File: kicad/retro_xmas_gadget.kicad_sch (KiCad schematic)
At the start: 83 parts, among them J1 USB_C_Receptacle_USB2.0_16P, J2 SD_Card_Receptacle, J3 AudioJack3_SwitchTR, J4 Conn_01x18, J5 Conn_01x02, J6 Conn_01x03, J7 Conn_01x03, J8 Conn_01x07, Q1 UMH3N, Q2 SS8050, Q3 PMOS, SW1 RESET, SW10 SELECT, SW11 START, SW12 A, SW13 B, SW2 BOOT, SW3 KH-SS12F23-G6, SW4 UP, SW5 DOWN, SW6 LEFT, SW7 RIGHT, SW8 MENU, SW9 OPTION, U1 CP2102N-Axx-xQFN28, U2 ESP32-S3-WROOM-1, U4 XC6210B332MR, U5 TP4056

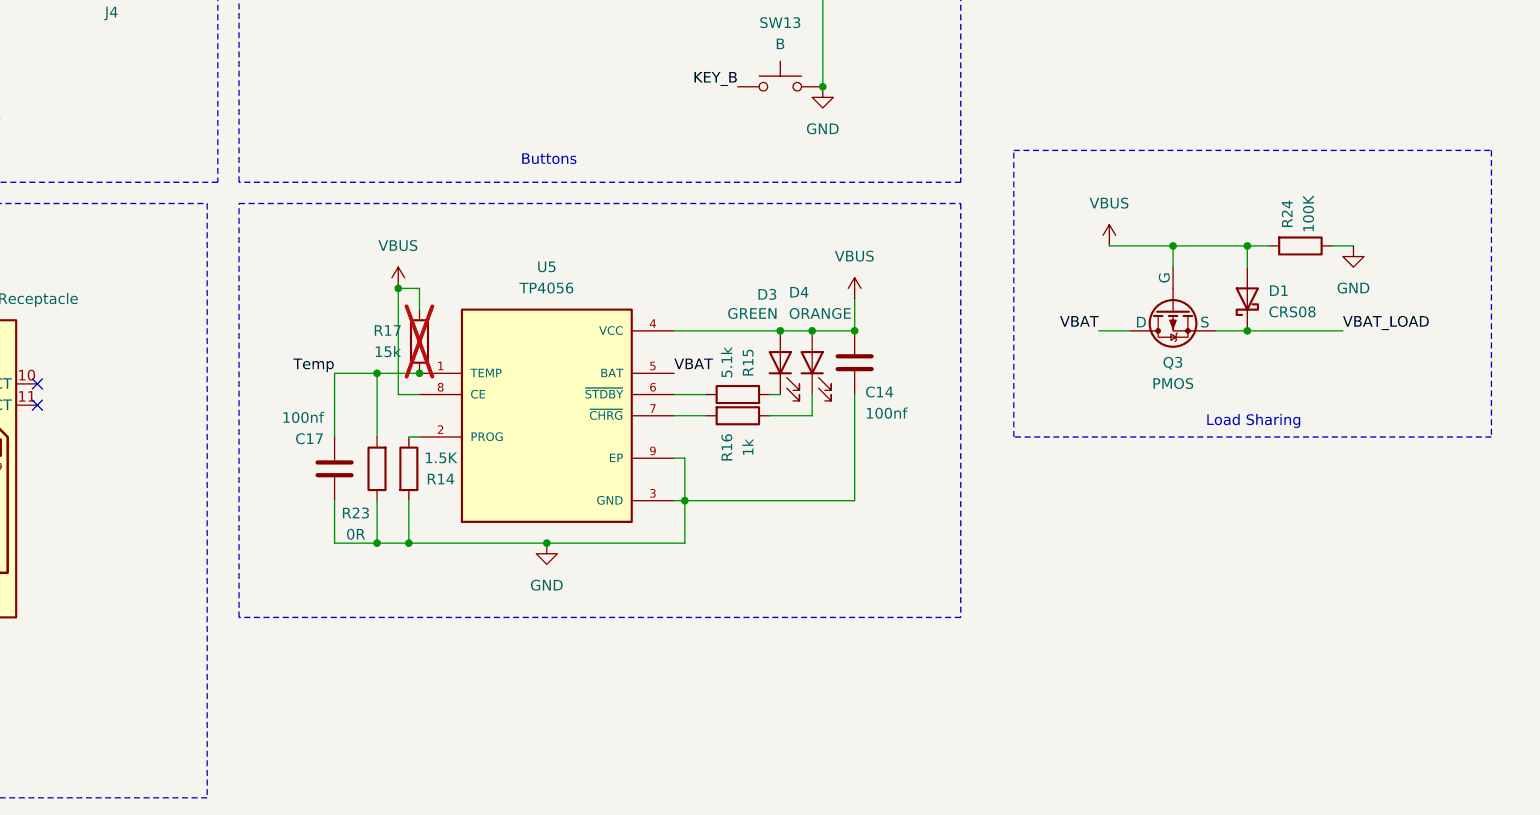
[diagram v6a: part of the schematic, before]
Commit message: footprint correction
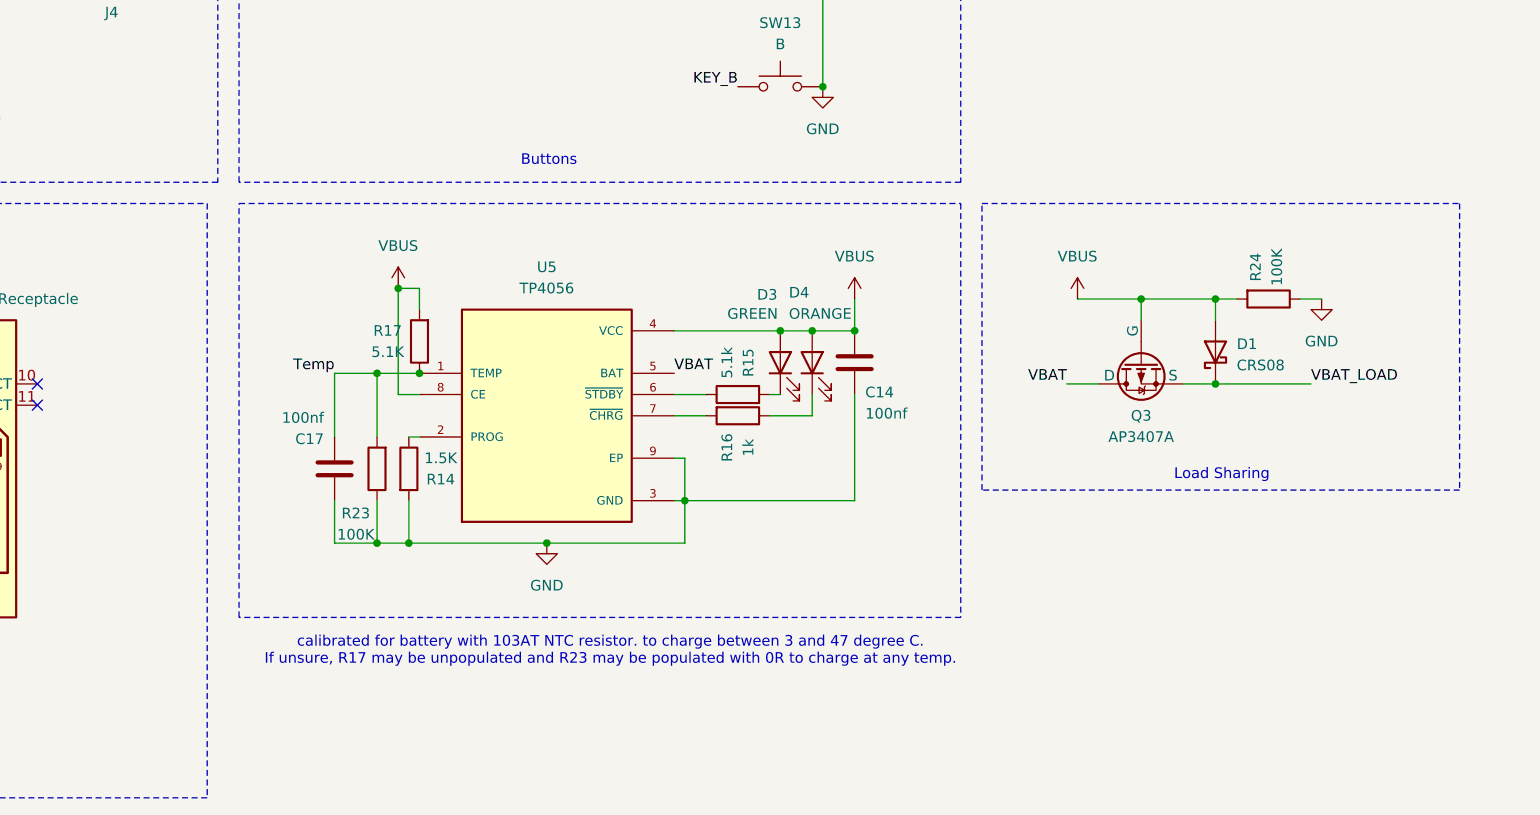
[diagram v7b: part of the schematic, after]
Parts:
- Q3: value PMOS -> AP3407A
- R17: value 15k -> 5.1K; now fitted
- R23: value 0R -> 100K
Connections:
- net VBAT: now also Q3.2 (D); no longer Q3.1 (D)
- net VBUS: now also Q3.1 (G); no longer Q3.2 (G)
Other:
- note added: "calibrated for battery with 103AT NTC resistor. to charge between 3 and 47 degree C. If unsure, R17 may be unpopulated and R23 may be populated with 0R to charge at any temp."
- moved on the sheet: D1, Q3, R24
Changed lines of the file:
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@@
 	)
 	(rectangle
-		(start 328.93 195.58)
-		(end 386.08 229.87)
+		(start 325.12 201.93)
+		(end 382.27 236.22)
 		(stroke
 			(width 0)
@@
 	(text "Load Sharing"
 		(exclude_from_sim no)
-		(at 357.632 228.092 0)
+		(at 353.822 234.442 0)
 		(effects
 			(font
@@
 		)
 	)
+	(text "calibrated for battery with 103AT NTC resistor. to charge between 3 and 47 degree C.\nIf unsure, R17 may be unpopulated and R23 may be populated with 0R to charge at any temp."
+		(exclude_from_sim no)
+		(at 280.67 255.524 0)
+		(effects
+			(font
+				(size 1.27 1.27)
+			)
+		)
+	)
 	(junction
 		(at 215.9 157.48)
@@
 	)
 	(junction
-		(at 356.87 217.17)
+		(at 353.06 223.52)
 		(diameter 0)
 		(color 0 0 0 0)
@@
 	)
 	(junction
-		(at 347.98 207.01)
+		(at 344.17 213.36)
 		(diameter 0)
 		(color 0 0 0 0)
@@
 	)
 	(junction
-		(at 356.87 207.01)
+		(at 353.06 213.36)
 		(diameter 0)
 		(color 0 0 0 0)
@@
 	(wire
 		(pts
-			(xy 369.57 207.01) (xy 367.03 207.01)
+			(xy 365.76 213.36) (xy 363.22 213.36)
 		)
 		(stroke
@@
 	(wire
 		(pts
-			(xy 356.87 207.01) (xy 347.98 207.01)
+			(xy 353.06 213.36) (xy 344.17 213.36)
 		)
 		(stroke
@@
 	(wire
 		(pts
-			(xy 347.98 207.01) (xy 347.98 209.55)
+			(xy 344.17 213.36) (xy 344.17 215.9)
 		)
 		(stroke
@@
 	(wire
 		(pts
-			(xy 340.36 207.01) (xy 347.98 207.01)
+			(xy 336.55 213.36) (xy 344.17 213.36)
 		)
 		(stroke
@@
 	(wire
 		(pts
-			(xy 359.41 207.01) (xy 356.87 207.01)
+			(xy 355.6 213.36) (xy 353.06 213.36)
 		)
 		(stroke
@@
 	(wire
 		(pts
-			(xy 356.87 209.55) (xy 356.87 207.01)
+			(xy 353.06 215.9) (xy 353.06 213.36)
 		)
 		(stroke
@@
 	(wire
 		(pts
-			(xy 353.06 217.17) (xy 356.87 217.17)
+			(xy 349.25 223.52) (xy 353.06 223.52)
 		)
 		(stroke
@@
 	(wire
 		(pts
-			(xy 356.87 217.17) (xy 368.3 217.17)
+			(xy 353.06 223.52) (xy 364.49 223.52)
 		)
 		(stroke
@@
 	(wire
 		(pts
-			(xy 342.9 217.17) (xy 339.09 217.17)
+			(xy 339.09 223.52) (xy 335.28 223.52)
 		)
 		(stroke
@@
 	)
 	(label "VBAT_LOAD"
-		(at 368.3 217.17 0)
+		(at 364.49 223.52 0)
 		(effects
 			(font
@@
 	)
 	(label "VBAT"
-		(at 339.09 217.17 180)
+		(at 335.28 223.52 180)
 		(effects
 			(font
@@
 	(symbol
 		(lib_id "power:VBUS")
-		(at 340.36 207.01 0)
+		(at 336.55 213.36 0)
 		(unit 1)
 		(exclude_from_sim no)
@@
 		(fields_autoplaced yes)
 		(property "Reference" "#PWR035"
-			(at 340.36 210.82 0)
+			(at 336.55 217.17 0)
 			(effects
 				(font
@@
 		)
 		(property "Value" "VBUS"
-			(at 340.36 201.93 0)
+			(at 336.55 208.28 0)
 			(effects
 				(font
@@
 		)
 		(property "Footprint" ""
-			(at 340.36 207.01 0)
+			(at 336.55 213.36 0)
 			(effects
 				(font
@@
 		)
 		(property "Datasheet" ""
-			(at 340.36 207.01 0)
+			(at 336.55 213.36 0)
 			(effects
 				(font
@@
 		)
 		(property "Description" "Power symbol creates a global label with name \"VBUS\""
-			(at 340.36 207.01 0)
+			(at 336.55 213.36 0)
 			(effects
 				(font
@@
 	(symbol
 		(lib_id "Device:R")
-		(at 363.22 207.01 270)
+		(at 359.41 213.36 270)
 		(unit 1)
 		(exclude_from_sim no)
@@
 		(dnp no)
 		(property "Reference" "R24"
-			(at 361.696 203.2 0)
+			(at 357.886 209.55 0)
 			(effects
 				(font
@@
 		)
 		(property "Value" "100K"
-			(at 364.236 203.2 0)
+			(at 360.426 209.55 0)
 			(effects
 				(font
@@
 		)
 		(property "Footprint" "Resistor_SMD:R_0603_1608Metric_Pad0.98x0.95mm_HandSolder"
-			(at 363.22 205.232 90)
+			(at 359.41 211.582 90)
 			(effects
 				(font
@@
 		)
 		(property "Datasheet" "~"
-			(at 363.22 207.01 0)
+			(at 359.41 213.36 0)
 			(effects
 				(font
@@
 		)
 		(property "Description" "Resistor"
-			(at 363.22 207.01 0)
+			(at 359.41 213.36 0)
 			(effects
 				(font
@@
 		(in_bom yes)
 		(on_board yes)
-		(dnp yes)
+		(dnp no)
 		(property "Reference" "R17"
 			(at 254 217.17 0)
@@
 			)
 		)
-		(property "Value" "15k"
+		(property "Value" "5.1K"
 			(at 254 219.71 0)
 			(effects
@@
 	(symbol
 		(lib_id "Device:D_Schottky")
-		(at 356.87 213.36 90)
+		(at 353.06 219.71 90)
 		(unit 1)
 		(exclude_from_sim no)
@@
 		(fields_autoplaced yes)
 		(property "Reference" "D1"
-			(at 359.41 212.4074 90)
+			(at 355.6 218.7574 90)
 			(effects
 				(font
@@
 		)
 		(property "Value" "CRS08"
-			(at 359.41 214.9474 90)
+			(at 355.6 221.2974 90)
 			(effects
 				(font
@@
 		)
 		(property "Footprint" "Diode_SMD:D_SOD-123"
-			(at 356.87 213.36 0)
+			(at 353.06 219.71 0)
 			(effects
 				(font
@@
 		)
 		(property "Datasheet" "~"
-			(at 356.87 213.36 0)
+			(at 353.06 219.71 0)
 			(effects
 				(font
@@
 		)
 		(property "Description" "Schottky diode"
-			(at 356.87 213.36 0)
+			(at 353.06 219.71 0)
 			(effects
 				(font
@@
 			)
 		)
-		(property "Value" "0R"
+		(property "Value" "100K"
 			(at 250.19 241.554 0)
 			(effects
@@
 	(symbol
 		(lib_id "Simulation_SPICE:PMOS")
-		(at 347.98 214.63 90)
+		(at 344.17 220.98 90)
 		(mirror x)
 		(unit 1)
@@
 		(dnp no)
 		(property "Reference" "Q3"
-			(at 347.98 220.98 90)
+			(at 344.17 227.33 90)
 			(effects
 				(font
@@
 			)
 		)
-		(property "Value" "PMOS"
-			(at 347.98 223.52 90)
+		(property "Value" "AP3407A"
+			(at 344.17 229.87 90)
 			(effects
 				(font
@@
 		)
 		(property "Footprint" "Package_TO_SOT_SMD:SOT-23_Handsoldering"
-			(at 345.44 219.71 0)
+			(at 341.63 226.06 0)
 			(effects
 				(font
@@
 		)
 		(property "Datasheet" "https://ngspice.sourceforge.io/docs/ngspice-html-manual/manual.xhtml#cha_MOSFETs"
-			(at 360.68 214.63 0)
+			(at 356.87 220.98 0)
 			(effects
 				(font
@@
 		)
 		(property "Description" "P-MOSFET transistor, drain/source/gate"
-			(at 347.98 214.63 0)
+			(at 344.17 220.98 0)
 			(effects
 				(font
@@
 		)
 		(property "Sim.Device" "PMOS"
-			(at 365.125 214.63 0)
+			(at 361.315 220.98 0)
 			(effects
 				(font
@@
 		)
 		(property "Sim.Type" "VDMOS"
-			(at 367.03 214.63 0)
+			(at 363.22 220.98 0)
 			(effects
 				(font
@@
 		)
 		(property "Sim.Pins" "1=D 2=G 3=S"
-			(at 363.22 214.63 0)
+			(at 359.41 220.98 0)
 			(effects
 				(font
@@
 	(symbol
 		(lib_id "power:GND")
-		(at 369.57 207.01 0)
+		(at 365.76 213.36 0)
 		(unit 1)
 		(exclude_from_sim no)
@@
 		(fields_autoplaced yes)
 		(property "Reference" "#PWR036"
-			(at 369.57 213.36 0)
+			(at 365.76 219.71 0)
 			(effects
 				(font
@@
 		)
 		(property "Value" "GND"
-			(at 369.57 212.09 0)
+			(at 365.76 218.44 0)
 			(effects
 				(font
@@
 		)
 		(property "Footprint" ""
-			(at 369.57 207.01 0)
+			(at 365.76 213.36 0)
 			(effects
 				(font
@@
 		)
 		(property "Datasheet" ""
-			(at 369.57 207.01 0)
+			(at 365.76 213.36 0)
 			(effects
 				(font
@@
 		)
 		(property "Description" "Power symbol creates a global label with name \"GND\" , ground"
-			(at 369.57 207.01 0)
+			(at 365.76 213.36 0)
 			(effects
 				(font

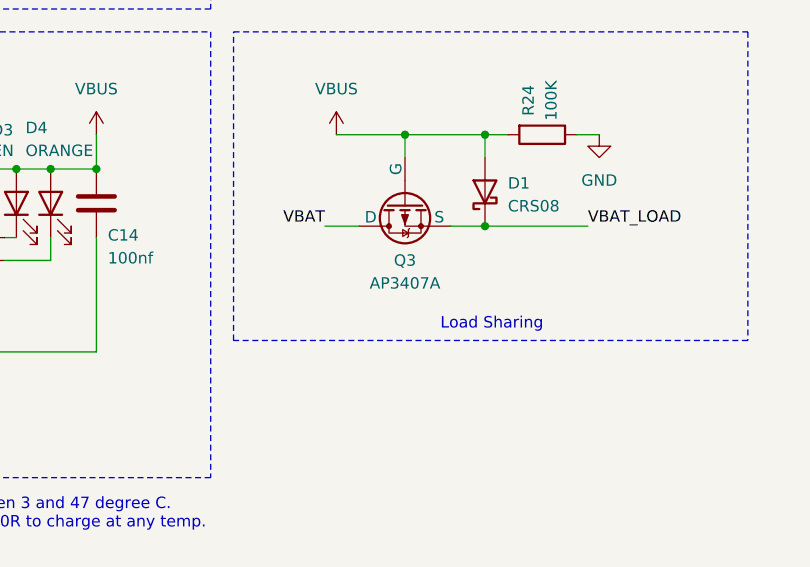
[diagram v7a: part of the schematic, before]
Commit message: component change
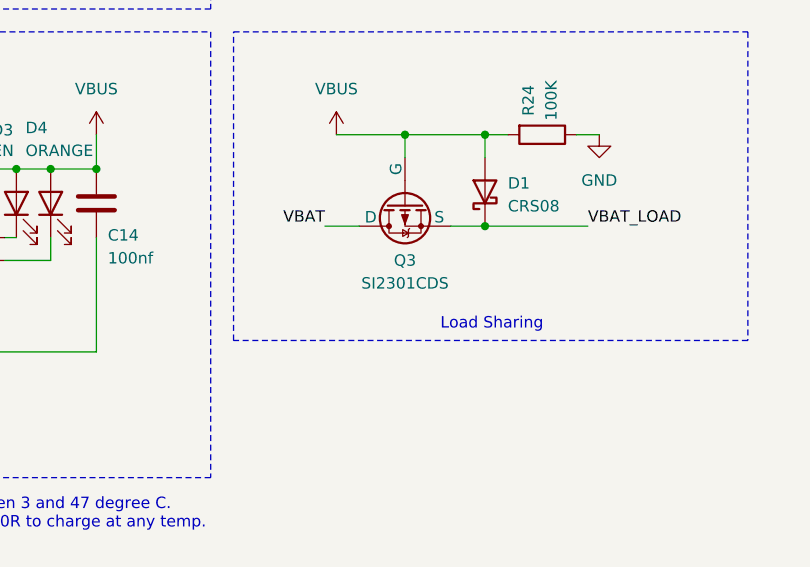
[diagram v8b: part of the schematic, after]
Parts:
- Q3: value AP3407A -> SI2301CDS
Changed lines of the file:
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@@
 			)
 		)
-		(property "Value" "AP3407A"
+		(property "Value" "SI2301CDS"
 			(at 344.17 229.87 90)
 			(effects
